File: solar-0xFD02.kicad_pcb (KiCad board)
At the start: 2 copper layers, 25.4 x 25.4 mm, 25 parts, among them J1 Solar, J2 BAT, J3 ESP32, Q1 MOSFET, U1 CN3801

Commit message: Cleanup
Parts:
- U1: footprint solar-0xFD02:CN3801 -> 0xFD:CN3801
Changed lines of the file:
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@@
     (add_net "Net-(U1-Pad4)")
   )
-  (module solar-0xFD02:CN3801 (layer F.Cu)
+  (module 0xFD:CN3801 (layer F.Cu)
     (at 140.335 83.312)
     (fp_text reference U1 (at 1.143 2.794) (layer F.SilkS)

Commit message: More cleanup
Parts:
- added C8: 100nF, Capacitor_SMD:C_1206_3216Metric_Pad1.33x1.80mm_HandSolder, B.Cu at (139.0, 87.6)
- added J4: BAT-, Connector_PinHeader_2.54mm:PinHeader_1x02_P2.54mm_Vertical, F.Cu at (147.8, 95.1)
- added Q2: P-Chan, Package_TO_SOT_SMD:SOT-23, B.Cu at (133.9, 92.3)
- added U2: NCP302HSN30, Package_TO_SOT_SMD:SOT-23-5, B.Cu at (139.2, 92.3)
- J3: renamed from J2; value BAT -> BAT+
- Q1: value MOSFET -> P-Chan
- moved C5 15.0 mm to (133.5, 87.6)
- moved J3 7.91 mm to (147.8, 88.1), turned to 180 degrees
- moved C3 2.04 mm to (144.0, 89.9)
- moved C4 1.66 mm to (141.4, 89.9)
- moved J2 0.18 mm to (147.8, 73.8)
- renumbered J3 to J2
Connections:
- C5 pad 1: /BAT+ -> /ESP-LOAD
- J2 pad 1: /BAT+ -> /ESP-LOAD
- J3 pad 1: /GND -> /BAT+
- R8 pad 1: /BAT+ -> /ESP-LOAD
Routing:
- net /ESP-LOAD: track 0.00 -> 40.0 mm
- net /Cd: track 0.00 -> 7.71 mm
- net /LVCO: track 0.00 -> 5.23 mm
- net /GND: track 99.6 -> 94.4 mm, vias 3 -> 5
- net /COM2: track 8.94 -> 7.91 mm
- net /BAT+: track 62.8 -> 62.0 mm
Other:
- board text added: "BAT+"
- board text added: "BAT-"
- board text removed: "+3.3v"
- board text removed: "LiFePo4 BAT"

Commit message: wip
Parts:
- added C9: 100nF, Capacitor_SMD:C_1206_3216Metric_Pad1.33x1.80mm_HandSolder, B.Cu at (138.9, 73.9)
- moved L1 5.52 mm to (135.4, 73.7), turned to 0 degrees
- moved R5 2.43 mm to (141.9, 73.7), turned to 180 degrees
- moved Q1 1.05 mm to (135.4, 77.3), turned to 90 degrees
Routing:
- net /DRAIN2: track 17.3 -> 10.1 mm
- net /ESP-LOAD: track 40.0 -> 35.0 mm
- net /CSP: track 11.9 -> 14.9 mm
- net /ADC: track 11.9 -> 14.6 mm
- net /DRV: track 8.03 -> 10.1 mm
- net /SOL+: track 53.9 -> 51.8 mm
- net /DRAIN: track 5.22 -> 6.48 mm
- net /MPPT: track 21.6 -> 22.4 mm
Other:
- board text added: "0xFD02"

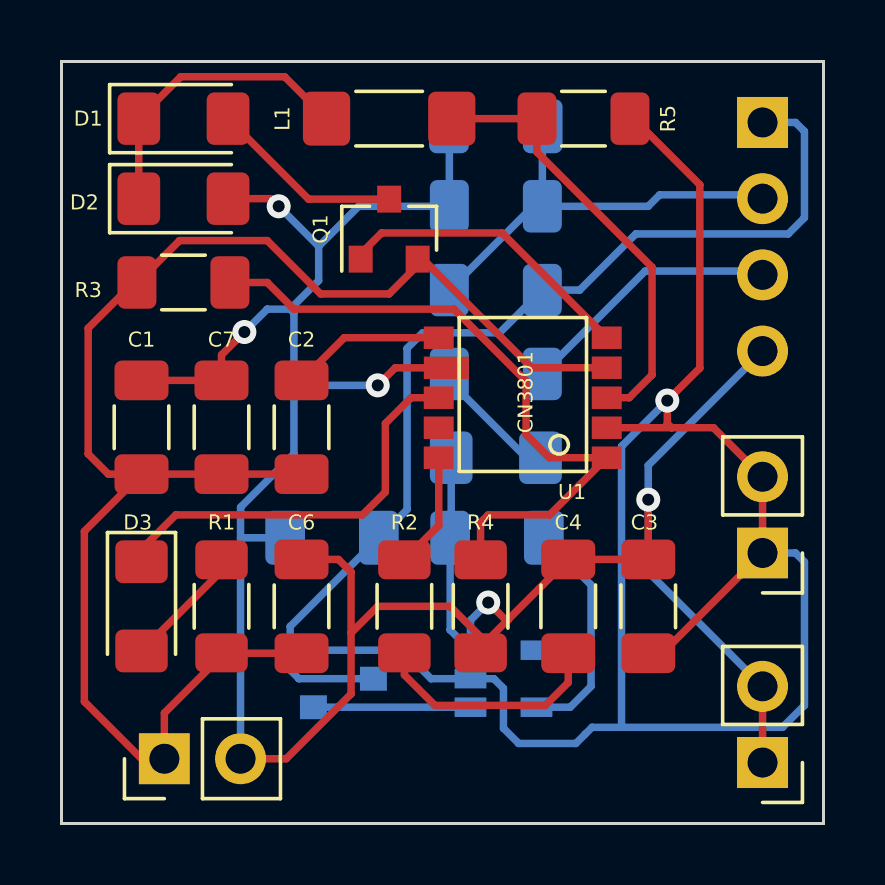
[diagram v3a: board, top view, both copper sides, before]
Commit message: Added Zener diode and resistor for low voltage cutoff
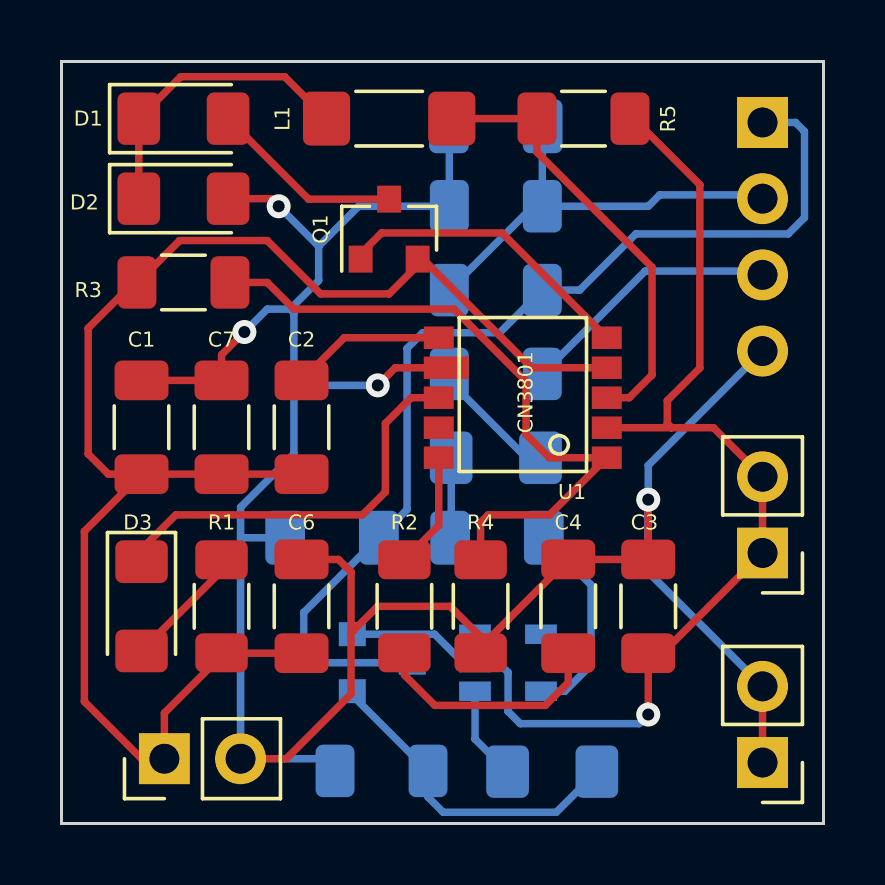
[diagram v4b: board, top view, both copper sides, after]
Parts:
- added D5: D_Zener, Diode_SMD:D_1206_3216Metric_Pad1.42x1.75mm_HandSolder, B.Cu at (140.8, 95.4)
- added R9: 10k, Resistor_SMD:R_1206_3216Metric_Pad1.30x1.75mm_HandSolder, B.Cu at (135.1, 95.4)
- moved Q2 1.40 mm to (135.2, 91.8)
- moved U2 0.55 mm to (139.3, 91.8)
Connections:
- U2 pad 1: /LVCO -> Net-(D5-Pad1)
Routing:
- net /BAT+: track 62.3 -> 39.5 mm
- net /LVCO: track 5.23 -> 11.3 mm
- net Net-(D5-Pad1): track 0.00 -> 3.13 mm
- net /GND: track 94.4 -> 91.7 mm, vias 5 -> 4
- net /Cd: track 7.71 -> 6.92 mm

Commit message: Updated annotations
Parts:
- renumbered C6 to C1, C1 to C2, C7 to C3, C2 to C4, C3 to C5, C4 to C6, C8 to C7, C9 to C8, C5 to C9, D5 to D4, D4 to D5, J3 to J2, J4 to J3, J2 to J4, R5 to R1, R1 to R2, R2 to R5, R9 to R6, R6 to R8, R8 to R9
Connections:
- net /COM2 renamed Net-(C6-Pad1)

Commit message: improvements and optimizations
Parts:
- added C5: 10uF, Capacitor_SMD:CP_Elec_3x5.4, F.Cu at (143.2, 74.0)
- added D4: LED, LED_SMD:LED_1206_3216Metric_Pad1.42x1.75mm_HandSolder, F.Cu at (134.9, 89.8)
- C1: footprint Capacitor_SMD:C_1206_3216Metric_Pad1.33x1.80mm_HandSolder -> Capacitor_SMD:CP_Elec_3x5.4
- C6: renamed from C5; value 22uF -> 10uF
- L1: footprint Inductor_SMD:L_1806_4516Metric_Pad1.57x1.80mm_HandSolder -> 0xFD:L-TYA4020
- moved C1 5.74 mm to (126.7, 89.9), turned to 270 degrees
- moved D3 5.23 mm to (132.4, 89.8)
- moved R5 4.16 mm to (142.2, 91.6)
- moved R1 3.93 mm to (143.3, 77.3)
- moved Q1 3.50 mm to (138.5, 78.9), turned to 180 degrees
- moved C7 2.30 mm to (139.8, 91.6)
- moved R4 2.16 mm to (137.3, 91.5)
- moved D2 2.12 mm to (127.1, 74.8), turned to 270 degrees
- moved C6 1.84 mm to (144.7, 91.6)
- moved D1 1.78 mm to (129.9, 74.8), turned to 270 degrees
- moved L1 1.11 mm to (135.2, 72.6), turned to 90 degrees
- moved U1 0.98 mm to (139.9, 84.2)
- moved J2 0.60 mm to (147.8, 87.5)
- moved R2 0.14 mm to (129.9, 89.8), turned to 270 degrees
- renumbered C9 to C10, C6 to C7, C7 to C8, C8 to C9, D4 to D5, D5 to D6, R5 to R4, R4 to R5
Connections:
- net Net-(C6-Pad1) renamed /COM2
- U1 pad 4: Net-(U1-Pad4) -> /DONE
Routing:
- net /GND: track 91.7 -> 129.6 mm, vias 4 -> 5
- net /CHRG: track 13.8 -> 6.68 mm
- net /DRV: track 10.1 -> 3.76 mm
- net /COM2: track 7.91 -> 2.40 mm
- net /DONE: track 0.00 -> 4.52 mm
- net /DRAIN2: track 10.1 -> 6.56 mm
- net /BAT+: track 39.5 -> 42.5 mm
- net /MPPT: track 22.4 -> 19.9 mm
- net /DRAIN: track 6.48 -> 8.64 mm
- net /SOL+: track 51.8 -> 50.7 mm
- net /CHRGLED: track 4.49 -> 5.29 mm
- net /VG: track 5.16 -> 4.39 mm
- net /COM: track 3.88 -> 4.42 mm

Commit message: no message
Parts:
- moved C1 6.05 mm to (126.7, 83.8), turned to 90 degrees
- moved C2 2.97 mm to (130.1, 83.9)
- moved C4 2.87 mm to (135.3, 84.0)
- moved C3 2.87 mm to (132.7, 83.9)
- moved U1 1.90 mm to (141.7, 84.8)
- moved J1 1.41 mm to (126.5, 95.1)
- moved R2 0.81 mm to (129.2, 90.1)
- moved D3 0.71 mm to (131.7, 90.2)
- moved D4 0.66 mm to (134.3, 90.2)
- moved Q1 0.26 mm to (138.3, 78.9)
- moved R4 0.07 mm to (137.3, 91.6)
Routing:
- net /CHRG: track 6.68 -> 11.8 mm
- net /MPPT: track 19.9 -> 22.3 mm
- net /DRV: track 3.76 -> 6.08 mm
- net /SOL+: track 50.7 -> 52.9 mm
- net /DONE: track 4.52 -> 6.69 mm
- net /GND: track 129.6 -> 127.8 mm, vias 5 -> 4
- net /BAT+: track 42.5 -> 41.0 mm
- net /CSP: track 15.4 -> 16.7 mm
- net /VG: track 4.39 -> 3.15 mm

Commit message: no message
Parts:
- moved R9 5.13 mm to (138.9, 74.2)
- moved C9 3.15 mm to (138.9, 77.1)
- moved R7 2.95 mm to (138.9, 79.5)
- moved D5 1.00 mm to (139.9, 95.1)
- moved R6 0.67 mm to (134.5, 95.1)
- moved Q2 0.33 mm to (135.0, 91.5)
- moved U2 0.31 mm to (139.5, 91.5)
- moved R8 0.28 mm to (139.0, 82.4)
- turned D6 to 180 degrees
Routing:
- net /GND: track 127.8 -> 134.9 mm
- net /ESP-LOAD: track 34.9 -> 37.2 mm
- net /BAT+: track 41.0 -> 42.9 mm
- net /ESP-LED2: track 4.57 -> 3.50 mm
